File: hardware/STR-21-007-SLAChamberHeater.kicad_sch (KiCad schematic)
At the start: 0 parts

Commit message: started sheet
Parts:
- added F?: Polyfuse, symbol Device:Polyfuse
- added J?: 12Vin, symbol Connector:Screw_Terminal_01x02
- added U?: TVS1800DRV, Package_SON:WSON-6-1EP_2x2mm_P0.65mm_EP1x1.6mm, symbol Power_Protection:TVS1800DRV
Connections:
- new net: F?.1, U?.4 (IN), U?.5 (IN), U?.6 (IN)
- new net: F?.2, J?.1 (Pin_1)
- new net GND: J?.2 (Pin_2), U?.1 (GND), U?.2 (GND), U?.3 (GND), U?.7 (GND)
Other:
- note added: "+"
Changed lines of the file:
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@@
     (comment 3 "License: CERN-OHL-P")
   )
-  (symbol_instances)
+  (wire (pts (xy 53.34 38.1) (xy 59.69 38.1))
+    (stroke (width 0) (type default) (color 0 0 0 0))
+  )
+  (wire (pts (xy 41.91 38.1) (xy 45.72 38.1))
+    (stroke (width 0) (type default) (color 0 0 0 0))
+  )
+  (wire (pts (xy 41.91 40.64) (xy 41.91 41.91))
+    (stroke (width 0) (type default) (color 0 0 0 0))
+  )
+  (wire (pts (xy 59.69 38.1) (xy 59.69 40.64))
+    (stroke (width 0) (type default) (color 0 0 0 0))
+  )
+  (wire (pts (xy 59.69 55.88) (xy 59.69 57.15))
+    (stroke (width 0) (type default) (color 0 0 0 0))
+  )
+  (text "+" (at 33.02 38.1 0)
+    (effects (font (size 1.27 1.27)) (justify left bottom))
+  )
+  (symbol (lib_id "Power_Protection:TVS1800DRV") (at 59.69 48.26 0) (unit 1)
+    (in_bom yes) (on_board yes) (fields_autoplaced)
+    (property "Reference" "U?" (id 0) (at 62.992 47.4253 0)
+      (effects (font (size 1.27 1.27)) (justify left))
+    )
+    (property "Value" "TVS1800DRV" (id 1) (at 62.992 49.9622 0)
+      (effects (font (size 1.27 1.27)) (justify left))
+    )
+    (property "Footprint" "Package_SON:WSON-6-1EP_2x2mm_P0.65mm_EP1x1.6mm" (id 2) (at 64.77 57.15 0)
+      (effects (font (size 1.27 1.27)) hide)
+    )
+    (property "Datasheet" "http://www.ti.com/lit/ds/symlink/tvs1800.pdf" (id 3) (at 57.15 48.26 0)
+      (effects (font (size 1.27 1.27)) hide)
+    )
+    (pin "1")
+    (pin "2")
+    (pin "3")
+    (pin "4")
+    (pin "5")
+    (pin "6")
+    (pin "7")
+  )
+  (symbol (lib_id "power:GND") (at 41.91 41.91 0) (unit 1)
+    (in_bom yes) (on_board yes) (fields_autoplaced)
+    (property "Reference" "#PWR?" (id 0) (at 41.91 48.26 0)
+      (effects (font (size 1.27 1.27)) hide)
+    )
+    (property "Value" "GND" (id 1) (at 41.91 46.3534 0))
+    (property "Footprint" "" (id 2) (at 41.91 41.91 0)
+      (effects (font (size 1.27 1.27)) hide)
+    )
+    (property "Datasheet" "" (id 3) (at 41.91 41.91 0)
+      (effects (font (size 1.27 1.27)) hide)
+    )
+    (pin "1")
+  )
+  (symbol (lib_id "Device:Polyfuse") (at 49.53 38.1 270) (unit 1)
+    (in_bom yes) (on_board yes) (fields_autoplaced)
+    (property "Reference" "F?" (id 0) (at 49.53 33.0032 90))
+    (property "Value" "Polyfuse" (id 1) (at 49.53 35.5401 90))
+    (property "Footprint" "" (id 2) (at 44.45 39.37 0)
+      (effects (font (size 1.27 1.27)) (justify left) hide)
+    )
+    (property "Datasheet" "~" (id 3) (at 49.53 38.1 0)
+      (effects (font (size 1.27 1.27)) hide)
+    )
+    (pin "1")
+    (pin "2")
+  )
+  (symbol (lib_id "Connector:Screw_Terminal_01x02") (at 36.83 38.1 0) (mirror y) (unit 1)
+    (in_bom yes) (on_board yes) (fields_autoplaced)
+    (property "Reference" "J?" (id 0) (at 36.83 33.1302 0))
+    (property "Value" "12Vin" (id 1) (at 36.83 35.6671 0))
+    (property "Footprint" "" (id 2) (at 36.83 38.1 0)
+      (effects (font (size 1.27 1.27)) hide)
+    )
+    (property "Datasheet" "~" (id 3) (at 36.83 38.1 0)
+      (effects (font (size 1.27 1.27)) hide)
+    )
+    (pin "1")
+    (pin "2")
+  )
+  (symbol (lib_id "power:GND") (at 59.69 57.15 0) (unit 1)
+    (in_bom yes) (on_board yes) (fields_autoplaced)
+    (property "Reference" "#PWR?" (id 0) (at 59.69 63.5 0)
+      (effects (font (size 1.27 1.27)) hide)
+    )
+    (property "Value" "GND" (id 1) (at 59.69 61.5934 0))
+    (property "Footprint" "" (id 2) (at 59.69 57.15 0)
+      (effects (font (size 1.27 1.27)) hide)
+    )
+    (property "Datasheet" "" (id 3) (at 59.69 57.15 0)
+      (effects (font (size 1.27 1.27)) hide)
+    )
+    (pin "1")
+  )
+  (sheet_instances
+    (path "/" (page "1"))
+  )
+  (symbol_instances
+    (path "/32385f38-d2c1-48c5-ad21-fcb8b5c8ebe4"
+      (reference "#PWR?") (unit 1) (value "GND") (footprint "")
+    )
+    (path "/8bc47c4b-57eb-4ae1-8a19-267b623254e2"
+      (reference "#PWR?") (unit 1) (value "GND") (footprint "")
+    )
+    (path "/36da2a73-c252-42ed-b969-b758fdb6438e"
+      (reference "F?") (unit 1) (value "Polyfuse") (footprint "")
+    )
+    (path "/7f9ee289-f15d-4a89-b40e-3217193ef6fc"
+      (reference "J?") (unit 1) (value "12Vin") (footprint "")
+    )
+    (path "/16238252-f909-4653-9048-4aaf17012347"
+      (reference "U?") (unit 1) (value "TVS1800DRV") (footprint "Package_SON:WSON-6-1EP_2x2mm_P0.65mm_EP1x1.6mm")
+    )
+  )
 )

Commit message: progress
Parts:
- removed F?: Polyfuse, symbol Device:Polyfuse
- removed J?: 12Vin, symbol Connector:Screw_Terminal_01x02
- removed U?: TVS1800DRV, Package_SON:WSON-6-1EP_2x2mm_P0.65mm_EP1x1.6mm, symbol Power_Protection:TVS1800DRV
- added C1, C2, C3, C?: C_Small, symbol Device:C_Small
- added C?: 22u, symbol Device:C_Small
- added C?: 100n, symbol Device:C_Small
- added C?: 10u, symbol Device:C_Small
- added D1: TVS 14.4V, symbol Device:D_Zener_Small
- added D?: LED_Small, symbol Device:LED_Small
- added F1: 6A, Fuse:Fuse_1206_3216Metric, symbol STR-Fuses:F1206HI8000V024TM
- added J?: JST, symbol Connector_Generic:Conn_01x02
- added J?: OLED 0.49, symbol Connector_Generic:Conn_01x14
- added J?: HEATER, symbol Connector:Screw_Terminal_01x02
- added J?: 2.5mm, symbol Connector:Barrel_Jack
- added J?: Prog 1.27mm, symbol Connector_Generic:Conn_02x03_Odd_Even
- added Q? (x2): Q_NMOS_DGS, symbol Device:Q_NMOS_DGS
- added Q?: Q_PMOS_DGS, symbol Device:Q_PMOS_DGS
- added R? (x3): 10K, symbol Device:R_Small
- added R? (x3): 100, symbol Device:R_Small
- added R?: R_Small, symbol Device:R_Small
- added U?: LM75B, symbol Sensor_Temperature:LM75B
- added U?: 3.3V DCDC, symbol Regulator_Linear:L7805
- added U?: ESP32-C3-MINI-1-N4, esp:ESP32-C3-MINI-1-N4, symbol STR-ESP32:ESP32-C3-MINI-1-N4
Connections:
- net GND: now also C1.2, C2.2, C3.2, C?.2, C?.2, C?.2, C?.2, D1.2 (A), J?.2, J?.2 (Pin_2), Q?.3 (S), Q?.3 (S), R?.2, R?.2, R?.2, U?.1 (GND), U?.11 (GND), U?.14 (GND), U?.2 (GND), U?.2 (GND), U?.36 (GND), U?.37 (GND), U?.38 (GND), U?.39 (GND), U?.4 (GND), U?.40 (GND), U?.41 (GND), U?.42 (GND), U?.43 (GND), U?.44 (GND), U?.45 (GND), U?.46 (GND), U?.47 (GND), U?.48 (GND), U?.49_1 (GND), U?.49_2 (GND), U?.49_3 (GND), U?.49_4 (GND), U?.49_5 (GND), U?.49_6 (GND), U?.49_7 (GND), U?.49_8 (GND), U?.49_9 (GND), U?.5 (A2), U?.50 (GND), U?.51 (GND), U?.52 (GND), U?.53 (GND), U?.6 (A1), U?.7 (A0)
- new net: Q?.2 (G), R?.1, R?.1 (x3)
- new net: D?.1 (K), Q?.1 (D)
- new net: D?.2 (A), R?.2
- new net: U?.10 (NC), U?.15 (NC), U?.17 (NC), U?.24 (NC), U?.25 (NC), U?.28 (NC), U?.29 (NC), U?.32 (NC), U?.33 (NC), U?.34 (NC), U?.35 (NC), U?.4 (NC), U?.7 (NC), U?.9 (NC)
- new net: J?.2 (Pin_2), Q?.1 (D)
- new net: J?.1 (Pin_1), Q?.3 (S)
- new net: F1.1, J?.1
- new net +12V: C1.1, C2.1, C3.1, C?.1, D1.1 (K), F1.2, J?.1 (Pin_1), Q?.1 (D), U?.1 (IN)
- new net +3V3: C?.1, C?.1, C?.1, R?.1, U?.3 (3V3), U?.3 (OUT), U?.8 (+Vs)
- new net HEATER_ON: R?.2
- new net HEATER_ON_LED: R?.2
- new net OVER_TEMP_EN: R?.2, U?.3 (O.S.)
- new net SCL: U?.2 (SCL)
- new net SDA: U?.1 (SDA)
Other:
- note added: "12VDC 5A Plugpack"
- note added: "20-30 DegC"
- note added: "30mm 12V Fan"
- note added: "Chamber Temperature"
- note added: "Heater"
- note added: "Heater Disable"
- note added: "OverTemp is set to 10 DegC Above controller Setpoint"
- note added: "PTC Heater 220DegC 12V ~4.7A max"

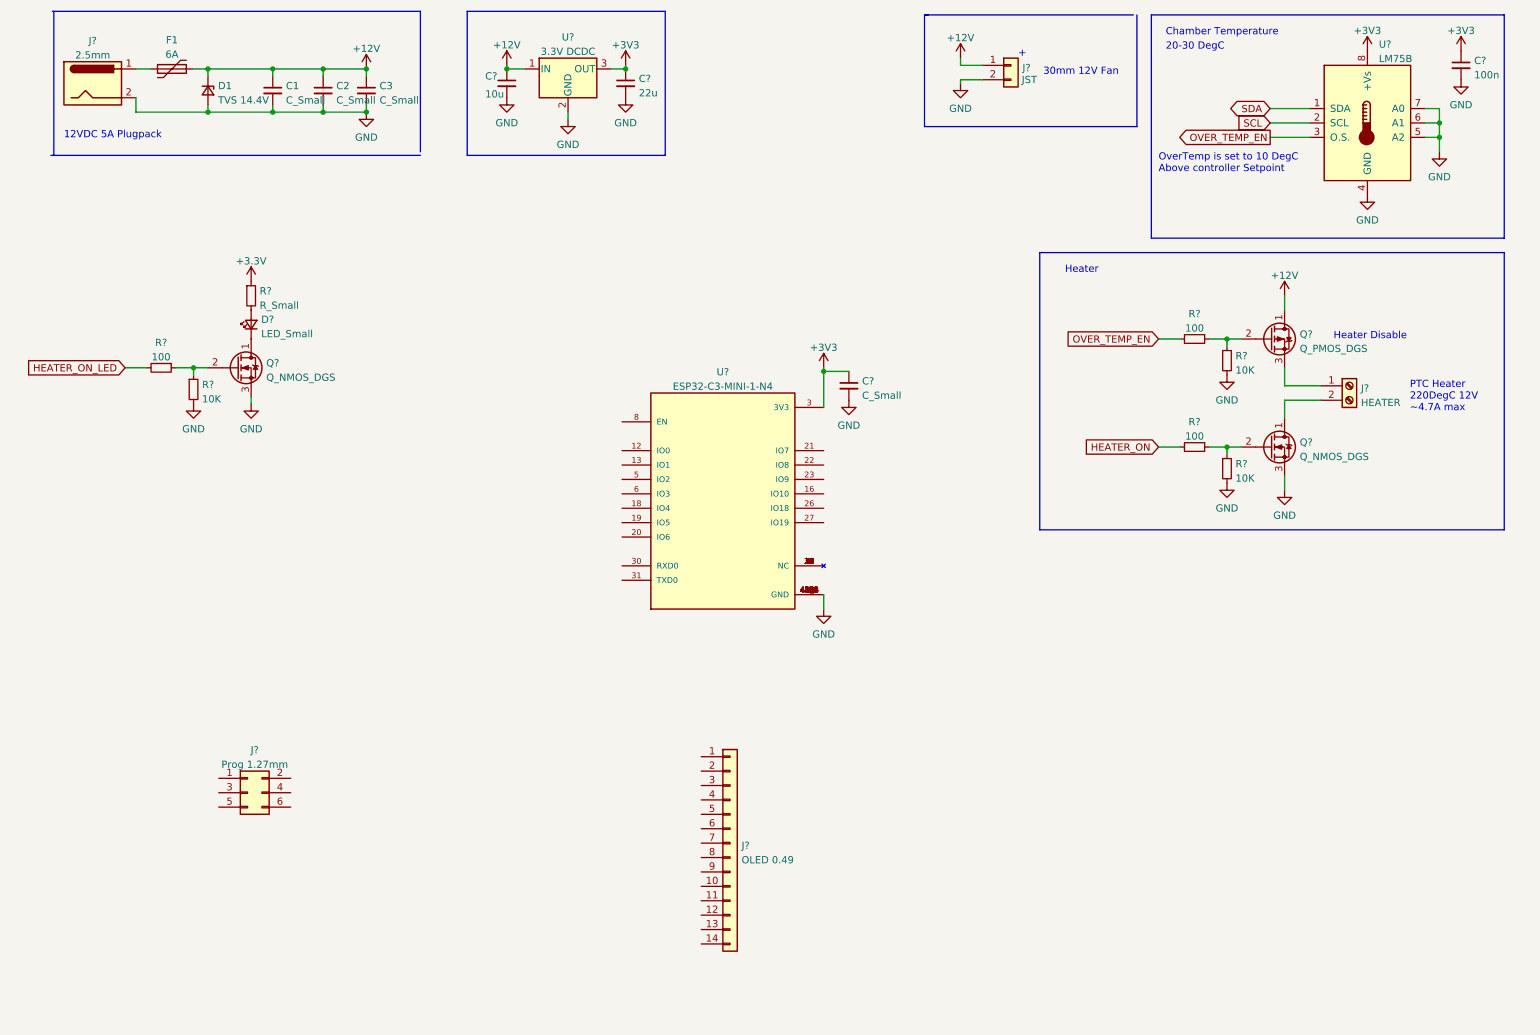
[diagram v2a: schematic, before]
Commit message: split out sheets
Fixed grid
Added datasheets
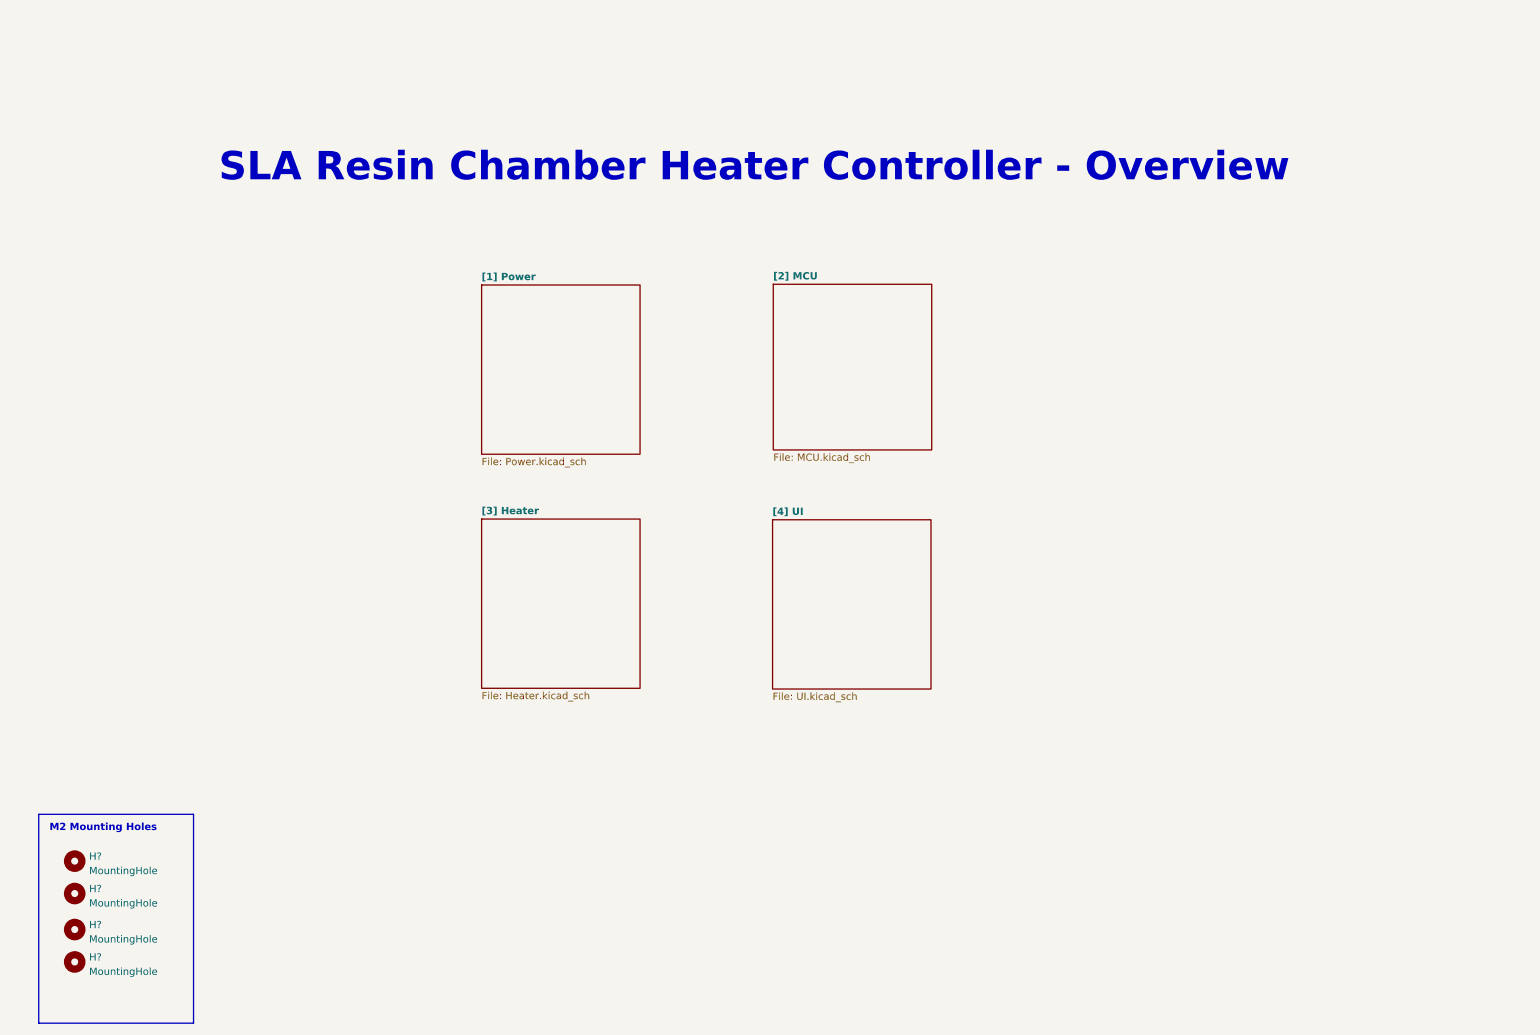
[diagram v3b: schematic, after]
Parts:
- removed C1, C2, C3, C?: C_Small, symbol Device:C_Small
- removed C?: 22u, symbol Device:C_Small
- removed C?: 100n, symbol Device:C_Small
- removed C?: 10u, symbol Device:C_Small
- removed D1: TVS 14.4V, symbol Device:D_Zener_Small
- removed D?: LED_Small, symbol Device:LED_Small
- removed F1: 6A, Fuse:Fuse_1206_3216Metric, symbol STR-Fuses:F1206HI8000V024TM
- removed J?: JST, symbol Connector_Generic:Conn_01x02
- removed J?: OLED 0.49, symbol Connector_Generic:Conn_01x14
- removed J?: HEATER, symbol Connector:Screw_Terminal_01x02
- removed J?: 2.5mm, symbol Connector:Barrel_Jack
- removed J?: Prog 1.27mm, symbol Connector_Generic:Conn_02x03_Odd_Even
- removed Q? (x2): Q_NMOS_DGS, symbol Device:Q_NMOS_DGS
- removed Q?: Q_PMOS_DGS, symbol Device:Q_PMOS_DGS
- removed R? (x3): 10K, symbol Device:R_Small
- removed R? (x3): 100, symbol Device:R_Small
- removed R?: R_Small, symbol Device:R_Small
- removed U?: LM75B, symbol Sensor_Temperature:LM75B
- removed U?: 3.3V DCDC, symbol Regulator_Linear:L7805
- removed U?: ESP32-C3-MINI-1-N4, esp:ESP32-C3-MINI-1-N4, symbol STR-ESP32:ESP32-C3-MINI-1-N4
- added H? (x4): MountingHole, MountingHole:MountingHole_2.2mm_M2, symbol Mechanical:MountingHole
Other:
- added sheet [1] Power (Power.kicad_sch)
- added sheet [2] MCU (MCU.kicad_sch)
- added sheet [3] Heater (Heater.kicad_sch)
- added sheet [4] UI (UI.kicad_sch)
- note added: "M2 Mounting Holes"
- note added: "SLA Resin Chamber Heater Controller - Overview"
- note removed: "+"
- note removed: "12VDC 5A Plugpack"
- note removed: "20-30 DegC"
- note removed: "30mm 12V Fan"
- note removed: "Chamber Temperature"
- note removed: "Heater"
- note removed: "Heater Disable"
- note removed: "OverTemp is set to 10 DegC Above controller Setpoint"
- note removed: "PTC Heater 220DegC 12V ~4.7A max"

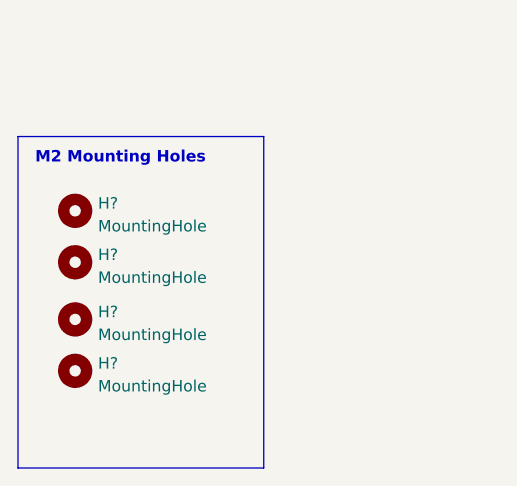
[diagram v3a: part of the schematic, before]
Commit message: schematics finished, footprints assigned. Still need to fix foorptints for MOSFETS
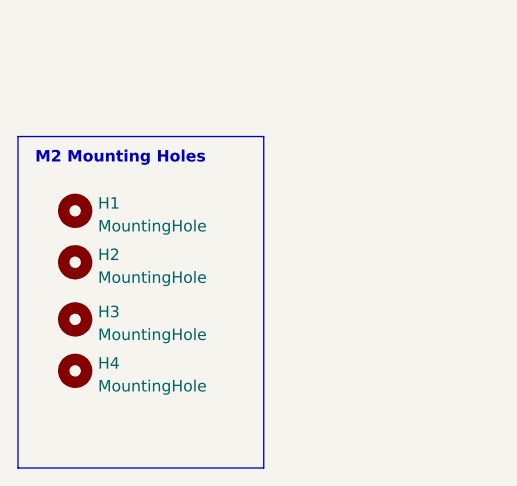
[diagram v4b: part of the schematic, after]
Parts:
- gave numbers to parts that had none: 4

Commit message: updated for kibot
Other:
- title: SLA Chamber Hearter for Resin Printers -> SLA Chamber Heater for Resin Printers
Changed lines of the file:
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@@
   (paper "A4")
   (title_block
-    (title "SLA Chamber Hearter for Resin Printers")
-    (date "2022-07-06")
-    (rev "A")
+    (title "SLA Chamber Heater for Resin Printers")
+    (date "%%date%%")
+    (rev "%%version%%")
     (comment 1 "Author: Stephen Eaton")
     (comment 2 "Project Github: https://github.com/madeinoz67/slachamberheater")
